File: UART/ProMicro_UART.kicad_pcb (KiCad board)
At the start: 2 copper layers, 17.8 x 33 mm, 57 parts, among them J2 Conn_01x06, J3 USB_B_Mini, U1 FT232H, U2 93CxxB, U3 AZ1117-3.3, Y1 12MHz

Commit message: dump
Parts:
- removed TP1: initials, Symbol:initials
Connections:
- net A0 renamed /TDI
- net A1 renamed /TDO
- net A2 renamed /TMS
- net A3 renamed /TCK
- net D0 renamed /TXD
- net D1 renamed /RXD
- net D10 renamed /CS0
- net D14 renamed /CIPO
- net D15 renamed /SCK
- net D16 renamed /COPI
- net D2 renamed /SDA
- net D3 renamed /SCL
- net D5 renamed /PWM
- net D9 renamed /CS1
- net Reset renamed /~RST
- A1 pad 24: +5V -> (no net)

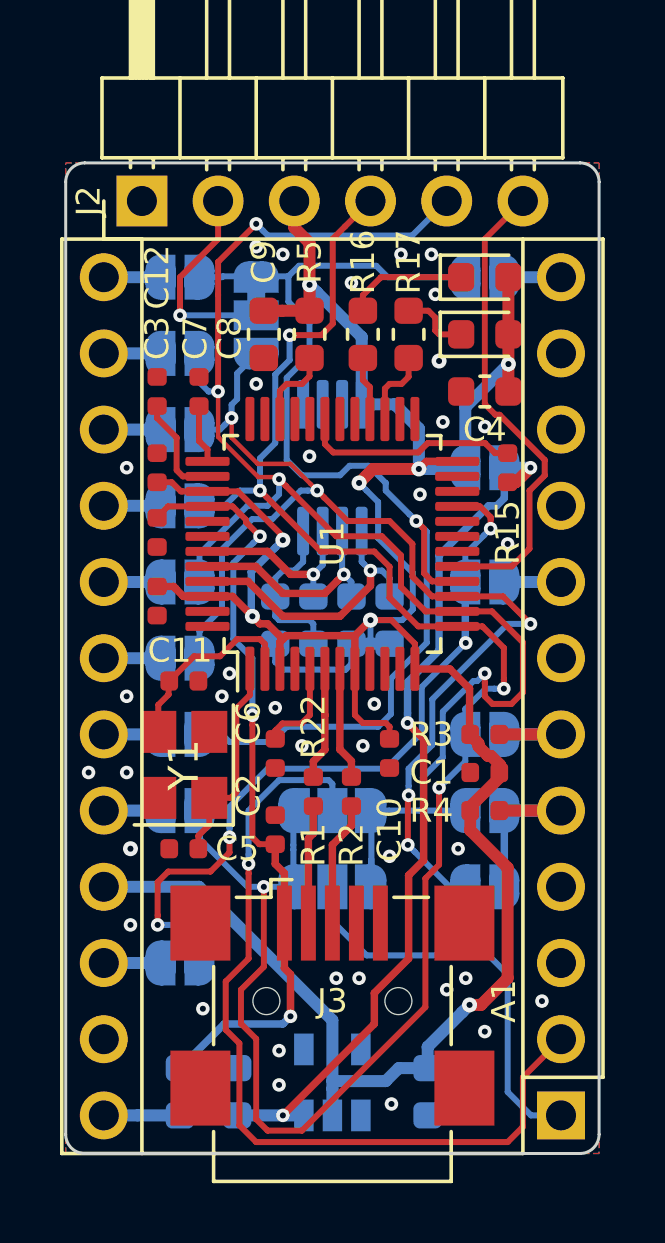
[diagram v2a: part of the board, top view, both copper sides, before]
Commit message: make controller holes wide enough
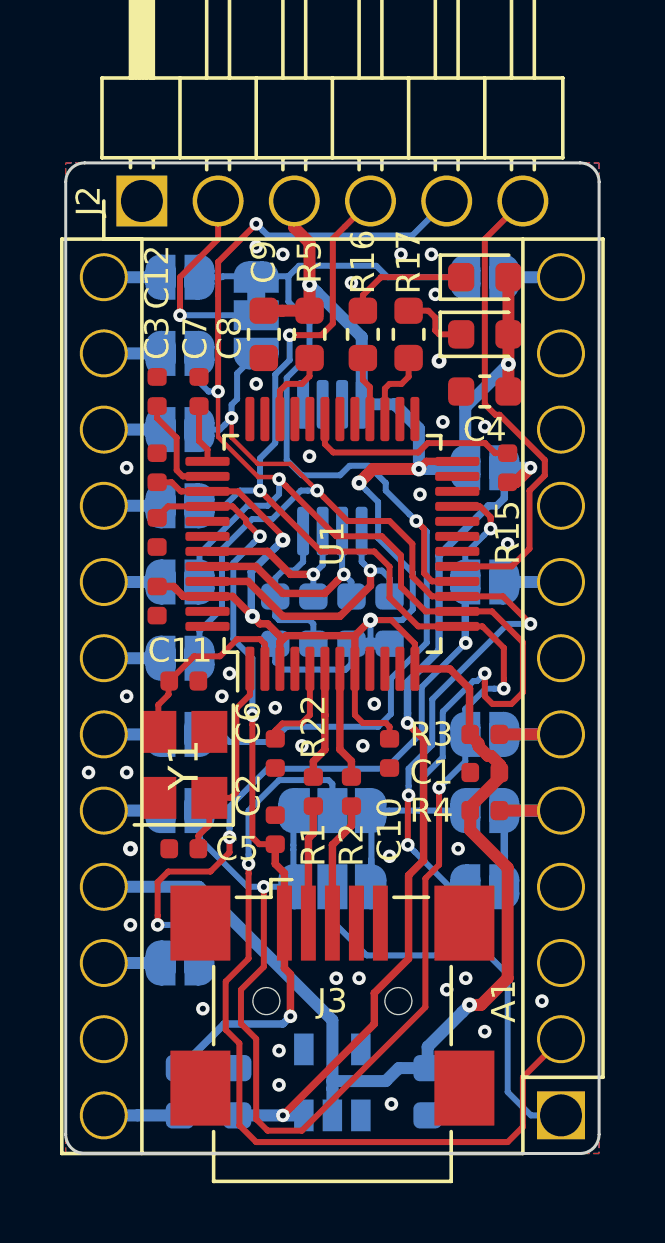
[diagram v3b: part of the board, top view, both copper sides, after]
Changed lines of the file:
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@@
-(kicad_pcb (version 20171130) (host pcbnew 5.1.5+dfsg1-2build2)
+(kicad_pcb (version 20171130) (host pcbnew 5.1.5)
   (general
     (thickness 1)
@@
     (fp_line (start 16.8 29.3) (end 16.8 -1.5) (layer F.CrtYd) (width 0.05))
     (fp_line (start 16.8 29.3) (end -1.5 29.3) (layer F.CrtYd) (width 0.05))
-    (pad 24 thru_hole oval (at 15.24 0 180) (size 1.6 1.6) (drill 1) (layers *.Cu *.Mask))
-    (pad 23 thru_hole oval (at 15.24 2.54 180) (size 1.6 1.6) (drill 1) (layers *.Cu *.Mask)
-      (net 1 GND))
-    (pad 22 thru_hole oval (at 15.24 5.08 180) (size 1.6 1.6) (drill 1) (layers *.Cu *.Mask)
+    (pad 24 thru_hole circle (at 15.24 0 180) (size 1.6 1.6) (drill 1.4) (layers *.Cu *.Mask))
+    (pad 23 thru_hole circle (at 15.24 2.54 180) (size 1.6 1.6) (drill 1.4) (layers *.Cu *.Mask)
+      (net 1 GND))
+    (pad 22 thru_hole circle (at 15.24 5.08 180) (size 1.6 1.6) (drill 1.4) (layers *.Cu *.Mask)
       (net 31 /~RST))
-    (pad 12 thru_hole oval (at 0 27.94 180) (size 1.6 1.6) (drill 1) (layers *.Cu *.Mask)
+    (pad 12 thru_hole circle (at 0 27.94 180) (size 1.6 1.6) (drill 1.4) (layers *.Cu *.Mask)
       (net 32 /CS1))
-    (pad 21 thru_hole oval (at 15.24 7.62 180) (size 1.6 1.6) (drill 1) (layers *.Cu *.Mask)
+    (pad 21 thru_hole circle (at 15.24 7.62 180) (size 1.6 1.6) (drill 1.4) (layers *.Cu *.Mask)
       (net 2 +3V3))
-    (pad 11 thru_hole oval (at 0 25.4 180) (size 1.6 1.6) (drill 1) (layers *.Cu *.Mask))
-    (pad 20 thru_hole oval (at 15.24 10.16 180) (size 1.6 1.6) (drill 1) (layers *.Cu *.Mask)
+    (pad 11 thru_hole circle (at 0 25.4 180) (size 1.6 1.6) (drill 1.4) (layers *.Cu *.Mask))
+    (pad 20 thru_hole circle (at 15.24 10.16 180) (size 1.6 1.6) (drill 1.4) (layers *.Cu *.Mask)
       (net 33 /TCK))
-    (pad 10 thru_hole oval (at 0 22.86 180) (size 1.6 1.6) (drill 1) (layers *.Cu *.Mask))
-    (pad 19 thru_hole oval (at 15.24 12.7 180) (size 1.6 1.6) (drill 1) (layers *.Cu *.Mask)
+    (pad 10 thru_hole circle (at 0 22.86 180) (size 1.6 1.6) (drill 1.4) (layers *.Cu *.Mask))
+    (pad 19 thru_hole circle (at 15.24 12.7 180) (size 1.6 1.6) (drill 1.4) (layers *.Cu *.Mask)
       (net 34 /TMS))
-    (pad 9 thru_hole oval (at 0 20.32 180) (size 1.6 1.6) (drill 1) (layers *.Cu *.Mask))
-    (pad 18 thru_hole oval (at 15.24 15.24 180) (size 1.6 1.6) (drill 1) (layers *.Cu *.Mask)
+    (pad 9 thru_hole circle (at 0 20.32 180) (size 1.6 1.6) (drill 1.4) (layers *.Cu *.Mask))
+    (pad 18 thru_hole circle (at 15.24 15.24 180) (size 1.6 1.6) (drill 1.4) (layers *.Cu *.Mask)
       (net 35 /TDO))
-    (pad 8 thru_hole oval (at 0 17.78 180) (size 1.6 1.6) (drill 1) (layers *.Cu *.Mask)
+    (pad 8 thru_hole circle (at 0 17.78 180) (size 1.6 1.6) (drill 1.4) (layers *.Cu *.Mask)
       (net 36 /PWM))
-    (pad 17 thru_hole oval (at 15.24 17.78 180) (size 1.6 1.6) (drill 1) (layers *.Cu *.Mask)
+    (pad 17 thru_hole circle (at 15.24 17.78 180) (size 1.6 1.6) (drill 1.4) (layers *.Cu *.Mask)
       (net 37 /TDI))
-    (pad 7 thru_hole oval (at 0 15.24 180) (size 1.6 1.6) (drill 1) (layers *.Cu *.Mask))
-    (pad 16 thru_hole oval (at 15.24 20.32 180) (size 1.6 1.6) (drill 1) (layers *.Cu *.Mask)
+    (pad 7 thru_hole circle (at 0 15.24 180) (size 1.6 1.6) (drill 1.4) (layers *.Cu *.Mask))
+    (pad 16 thru_hole circle (at 15.24 20.32 180) (size 1.6 1.6) (drill 1.4) (layers *.Cu *.Mask)
       (net 38 /SCK))
-    (pad 6 thru_hole oval (at 0 12.7 180) (size 1.6 1.6) (drill 1) (layers *.Cu *.Mask)
+    (pad 6 thru_hole circle (at 0 12.7 180) (size 1.6 1.6) (drill 1.4) (layers *.Cu *.Mask)
       (net 39 /SCL))
-    (pad 15 thru_hole oval (at 15.24 22.86 180) (size 1.6 1.6) (drill 1) (layers *.Cu *.Mask)
+    (pad 15 thru_hole circle (at 15.24 22.86 180) (size 1.6 1.6) (drill 1.4) (layers *.Cu *.Mask)
       (net 40 /CIPO))
-    (pad 5 thru_hole oval (at 0 10.16 180) (size 1.6 1.6) (drill 1) (layers *.Cu *.Mask)
+    (pad 5 thru_hole circle (at 0 10.16 180) (size 1.6 1.6) (drill 1.4) (layers *.Cu *.Mask)
       (net 41 /SDA))
-    (pad 14 thru_hole oval (at 15.24 25.4 180) (size 1.6 1.6) (drill 1) (layers *.Cu *.Mask)
+    (pad 14 thru_hole circle (at 15.24 25.4 180) (size 1.6 1.6) (drill 1.4) (layers *.Cu *.Mask)
       (net 42 /COPI))
-    (pad 4 thru_hole oval (at 0 7.62 180) (size 1.6 1.6) (drill 1) (layers *.Cu *.Mask)
-      (net 1 GND))
-    (pad 13 thru_hole oval (at 15.24 27.94 180) (size 1.6 1.6) (drill 1) (layers *.Cu *.Mask)
+    (pad 4 thru_hole circle (at 0 7.62 180) (size 1.6 1.6) (drill 1.4) (layers *.Cu *.Mask)
+      (net 1 GND))
+    (pad 13 thru_hole circle (at 15.24 27.94 180) (size 1.6 1.6) (drill 1.4) (layers *.Cu *.Mask)
       (net 43 /CS0))
-    (pad 3 thru_hole oval (at 0 5.08 180) (size 1.6 1.6) (drill 1) (layers *.Cu *.Mask))
-    (pad 2 thru_hole oval (at 0 2.54 180) (size 1.6 1.6) (drill 1) (layers *.Cu *.Mask)
+    (pad 3 thru_hole circle (at 0 5.08 180) (size 1.6 1.6) (drill 1.4) (layers *.Cu *.Mask))
+    (pad 2 thru_hole circle (at 0 2.54 180) (size 1.6 1.6) (drill 1.4) (layers *.Cu *.Mask)
       (net 44 /TXD))
-    (pad 1 thru_hole rect (at 0 0 180) (size 1.6 1.6) (drill 1) (layers *.Cu *.Mask)
+    (pad 1 thru_hole rect (at 0 0 180) (size 1.6 1.6) (drill 1.4) (layers *.Cu *.Mask)
       (net 45 /RXD))
     (model ${KISYS3DMOD}/Module.3dshapes/Sparkfun_Pro_Micro.wrl
@@
     (fp_line (start 4.04 -1.27) (end 4.04 13.97) (layer F.Fab) (width 0.1))
     (fp_line (start 2.135 -1.27) (end 4.04 -1.27) (layer F.Fab) (width 0.1))
-    (pad 6 thru_hole oval (at 0 12.7 90) (size 1.7 1.7) (drill 1) (layers *.Cu *.Mask)
+    (pad 6 thru_hole circle (at 0 12.7 90) (size 1.7 1.7) (drill 1.4) (layers *.Cu *.Mask)
       (net 20 ADBUS4))
-    (pad 5 thru_hole oval (at 0 10.16 90) (size 1.7 1.7) (drill 1) (layers *.Cu *.Mask)
+    (pad 5 thru_hole circle (at 0 10.16 90) (size 1.7 1.7) (drill 1.4) (layers *.Cu *.Mask)
       (net 30 ADBUS1))
-    (pad 4 thru_hole oval (at 0 7.62 90) (size 1.7 1.7) (drill 1) (layers *.Cu *.Mask)
+    (pad 4 thru_hole circle (at 0 7.62 90) (size 1.7 1.7) (drill 1.4) (layers *.Cu *.Mask)
       (net 3 ADBUS0))
-    (pad 3 thru_hole oval (at 0 5.08 90) (size 1.7 1.7) (drill 1) (layers *.Cu *.Mask)
+    (pad 3 thru_hole circle (at 0 5.08 90) (size 1.7 1.7) (drill 1.4) (layers *.Cu *.Mask)
       (net 2 +3V3))
-    (pad 2 thru_hole oval (at 0 2.54 90) (size 1.7 1.7) (drill 1) (layers *.Cu *.Mask)
+    (pad 2 thru_hole circle (at 0 2.54 90) (size 1.7 1.7) (drill 1.4) (layers *.Cu *.Mask)
       (net 27 "Net-(J2-Pad2)"))
-    (pad 1 thru_hole rect (at 0 0 90) (size 1.7 1.7) (drill 1) (layers *.Cu *.Mask)
+    (pad 1 thru_hole rect (at 0 0 90) (size 1.7 1.7) (drill 1.4) (layers *.Cu *.Mask)
       (net 1 GND))
     (model ${KISYS3DMOD}/Connector_PinHeader_2.54mm.3dshapes/PinHeader_1x06_P2.54mm_Horizontal.wrl

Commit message: update design
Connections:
- R1 pad 2: Net-(J3-Pad2) -> Net-(R1-Pad2)
- R2 pad 2: Net-(J3-Pad3) -> Net-(R2-Pad2)
- U1 pad 18: (no net) -> Net-(U1-Pad18)
- U1 pad 19: (no net) -> Net-(U1-Pad19)
- U1 pad 20: (no net) -> Net-(U1-Pad20)
- U1 pad 25: (no net) -> Net-(U1-Pad25)
- U1 pad 26: (no net) -> Net-(U1-Pad26)
- U1 pad 29: (no net) -> Net-(U1-Pad29)
- U1 pad 30: (no net) -> Net-(U1-Pad30)
- U1 pad 32: (no net) -> Net-(U1-Pad32)
- U1 pad 33: (no net) -> Net-(U1-Pad33)
- U2 pad 6: (no net) -> Net-(U2-Pad6)
- U2 pad 7: (no net) -> Net-(U2-Pad7)

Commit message: UART
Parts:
- moved J2 106.3 mm to (157.5, 87.6), turned to 0 degrees
- moved JP5 102.4 mm to (154.9, 88.9), turned to 90 degrees
- moved JP2 99.6 mm to (152.4, 88.9), turned to 90 degrees
- moved C7 98.9 mm to (151.1, 88.1), turned to 0 degrees
- moved JP16 98.8 mm to (153.7, 91.4), turned to 180 degrees
- moved C9 97.8 mm to (153.0, 91.7), turned to 180 degrees
- moved C8 97.6 mm to (151.1, 89.5), turned to 0 degrees
- moved JP3 96.8 mm to (149.9, 88.9), turned to 90 degrees
- moved R5 96.6 mm to (153.0, 93.2), turned to 0 degrees
- moved C12 96.2 mm to (148.6, 88.1), turned to 0 degrees
- moved R16 95.1 mm to (153.0, 95.0), turned to 0 degrees
- moved D1 94.3 mm to (154.9, 99.1), turned to 270 degrees
- moved JP4 94.3 mm to (154.9, 99.1), turned to 270 degrees
- moved JP1 94.1 mm to (147.3, 88.9), turned to 90 degrees
- moved C3 93.9 mm to (146.4, 88.1), turned to 180 degrees
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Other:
- board size 17.8 x 33 mm -> 33 x 17.8 mm
